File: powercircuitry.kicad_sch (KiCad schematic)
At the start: 160 parts, among them U1001 AM6231ASGGGAALW, U4001 TPS6521903RHBR, U4002 TLV62595DMQR

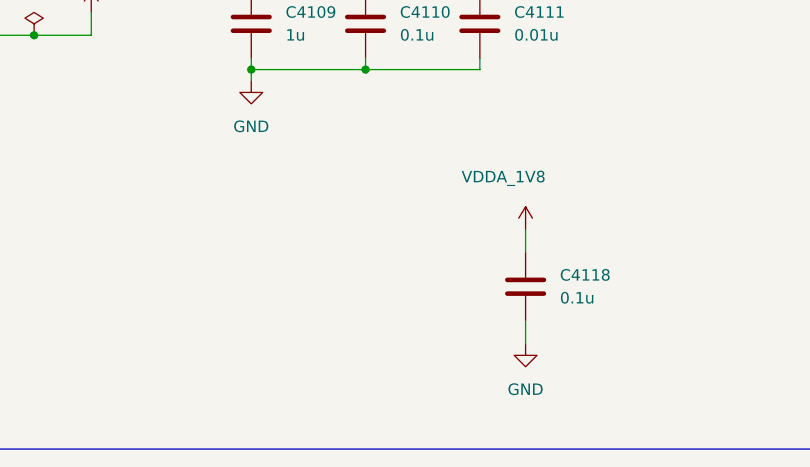
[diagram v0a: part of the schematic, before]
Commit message: More SoC decaps
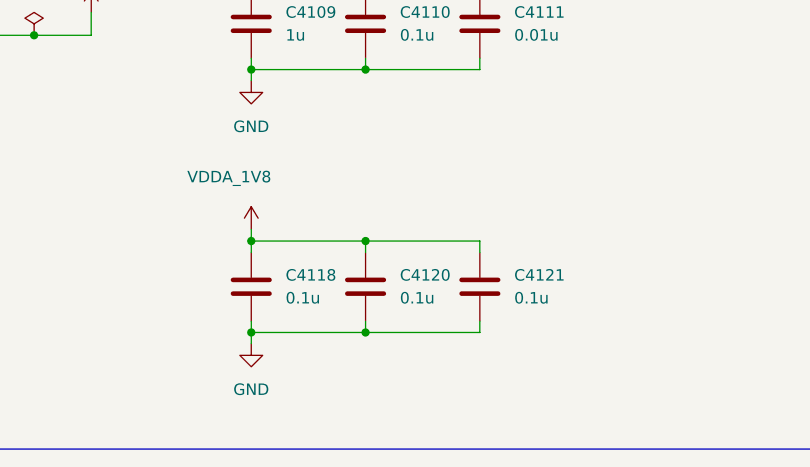
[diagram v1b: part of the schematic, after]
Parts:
- added C4120, C4121: 0.1u, Capacitor_SMD:C_0201_0603Metric, symbol Device:C
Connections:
- net GND: now also C4120.2, C4121.2
- net VDDA_1V8: now also C4120.1, C4121.1
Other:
- moved on the sheet: C4118

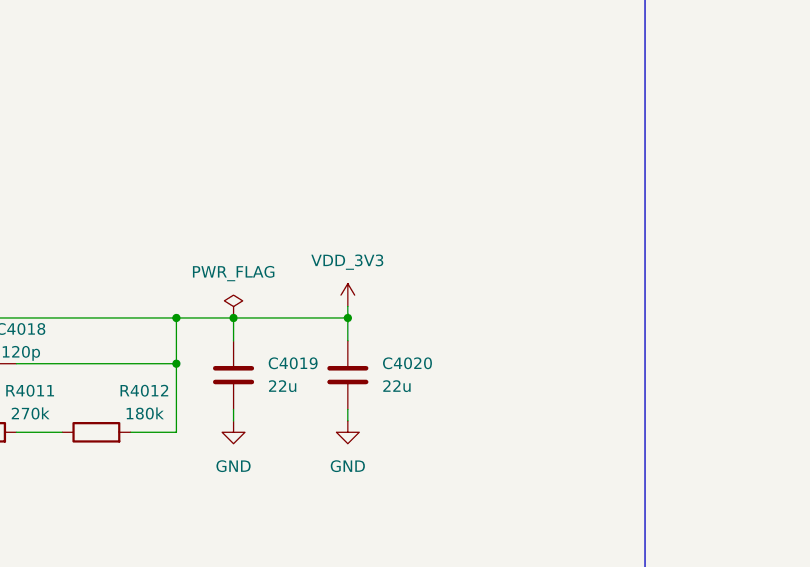
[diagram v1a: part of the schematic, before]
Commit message: Routed 5V -> 3.3V Buck converter and started PMIC routing and power planes
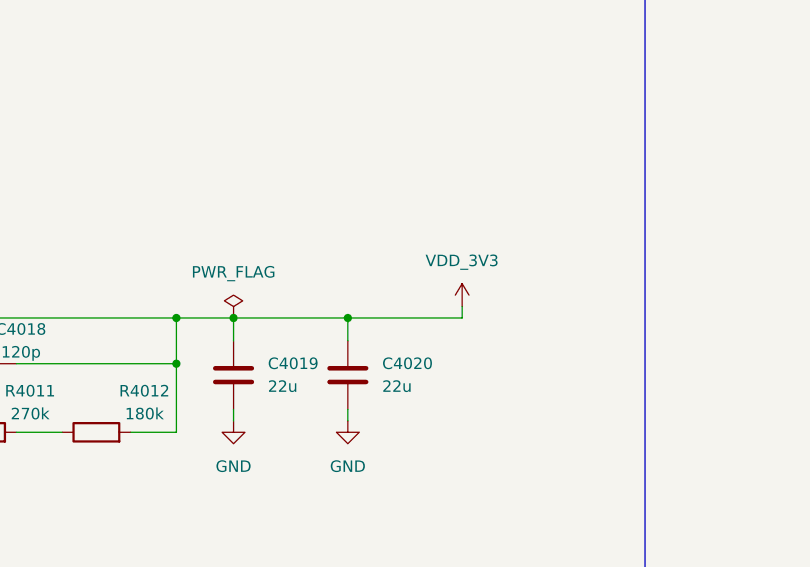
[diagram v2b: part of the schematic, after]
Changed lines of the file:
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@@
 	(wire
 		(pts
-			(xy 205.74 299.72) (xy 205.74 300.99)
+			(xy 218.44 299.72) (xy 218.44 300.99)
 		)
 		(stroke
@@
 	(wire
 		(pts
+			(xy 218.44 300.99) (xy 205.74 300.99)
+		)
+		(stroke
+			(width 0)
+			(type default)
+		)
+	)
+	(wire
+		(pts
 			(xy 538.48 431.8) (xy 538.48 434.34)
 		)
@@
 	(symbol
 		(lib_id "power:VDD")
-		(at 205.74 299.72 0)
+		(at 218.44 299.72 0)
 		(unit 1)
 		(exclude_from_sim no)
@@
 		(fields_autoplaced yes)
 		(property "Reference" "#PWR04067"
-			(at 205.74 303.53 0)
+			(at 218.44 303.53 0)
 			(effects
 				(font
@@
 		)
 		(property "Value" "VDD_3V3"
-			(at 205.74 294.64 0)
+			(at 218.44 294.64 0)
 			(effects
 				(font
@@
 		)
 		(property "Footprint" ""
-			(at 205.74 299.72 0)
+			(at 218.44 299.72 0)
 			(effects
 				(font
@@
 		)
 		(property "Datasheet" ""
-			(at 205.74 299.72 0)
+			(at 218.44 299.72 0)
 			(effects
 				(font
@@
 		)
 		(property "Description" "Power symbol creates a global label with name \"VDD\""
-			(at 205.74 299.72 0)
+			(at 218.44 299.72 0)
 			(effects
 				(font

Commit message: Routed out PMIC
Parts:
- removed C4010: 2.2u, Capacitor_SMD:C_0402_1005Metric, symbol Device:C
- removed R4001: 0R, Resistor_SMD:R_0402_1005Metric, symbol Device:R
- added C4122, C4123, C4124: 0.1u, Capacitor_SMD:C_0402_1005Metric, symbol Device:C
- C4009: value 2.2u -> 4.7u
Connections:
- net PMIC_B1_FB is gone; now on net VDD_CORE: U4001.1 (FB_B1)
- net GND: now also C4122.2, C4123.2, C4124.2
- net VSYS_5V: now also C4122.1, C4123.1, C4124.1
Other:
- moved on the sheet: C4001, C4003, C4005

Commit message: Continued PDN routing
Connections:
- net VDDA_0V85 renamed VDDR_CORE
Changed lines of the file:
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@@
 		(on_board yes)
 		(dnp no)
-		(fields_autoplaced yes)
 		(property "Reference" "#PWR04077"
 			(at 365.76 433.07 0)
@@
 			)
 		)
-		(property "Value" "VDDA_0V85"
-			(at 365.76 424.18 0)
+		(property "Value" "VDDR_CORE"
+			(at 361.442 424.18 0)
 			(effects
 				(font
 					(size 1.27 1.27)
 				)
+				(justify left)
 			)
 		)
@@
 		(on_board yes)
 		(dnp no)
-		(fields_autoplaced yes)
 		(property "Reference" "#PWR04020"
 			(at 414.02 182.88 0)
@@
 			)
 		)
-		(property "Value" "VDDA_0V85"
-			(at 414.02 173.99 0)
+		(property "Value" "VDDR_CORE"
+			(at 409.194 174.244 0)
 			(effects
 				(font
 					(size 1.27 1.27)
 				)
+				(justify left)
 			)
 		)
@@
 			)
 		)
-		(property "Value" "VDDA_0V85"
+		(property "Value" "VDDR_CORE"
 			(at 234.188 191.516 0)
 			(effects

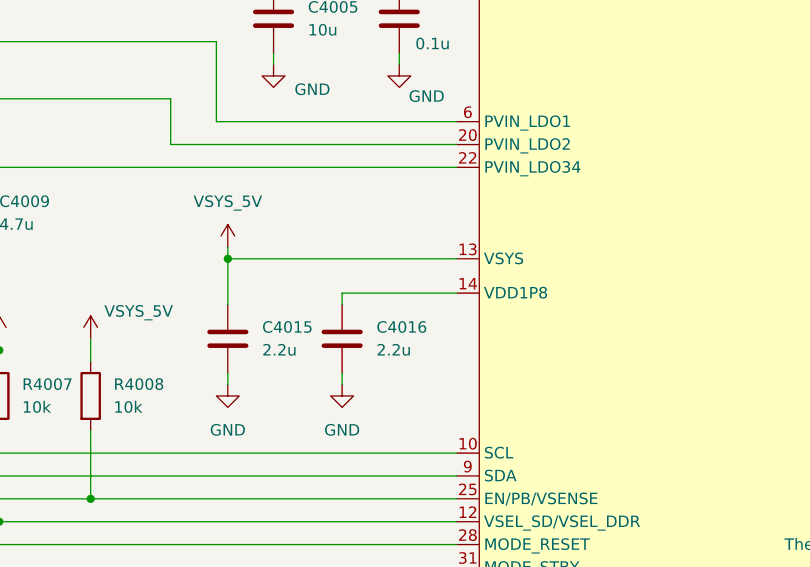
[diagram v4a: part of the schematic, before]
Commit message: Improved clock layout and clock PDN
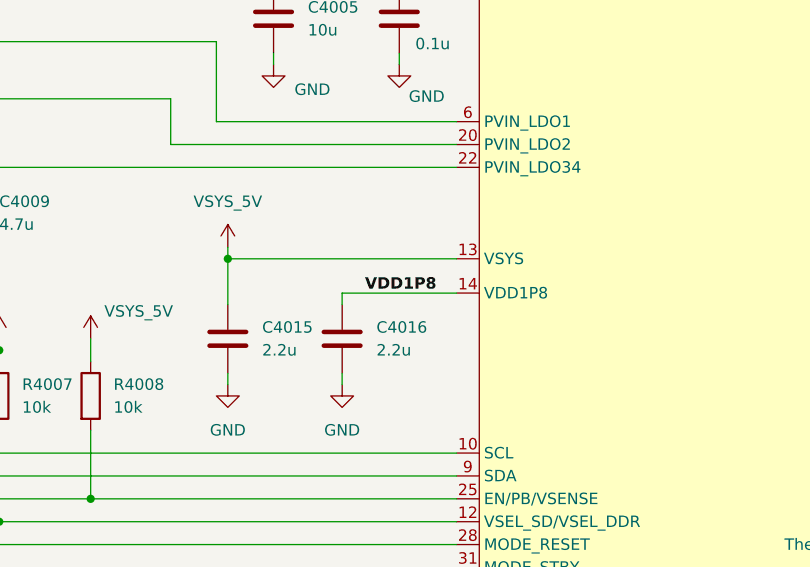
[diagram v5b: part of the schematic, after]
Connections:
- net VDD1P8: now reaches C4016.1, U4001.14 (VDD1P8)
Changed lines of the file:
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@@
+		)
+	)
+	(label "VDD1P8"
+		(at 154.94 214.63 0)
+		(effects
+			(font
+				(size 1.27 1.27)
+				(thickness 0.254)
+				(bold yes)
+			)
+			(justify left bottom)
 		)
 	)

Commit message: Added new radio schematic
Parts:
- renumbered C4001 to C3001, C4122 to C3002, C4002 to C3003, C4003 to C3004, C4123 to C3005, C4004 to C3006, C4005 to C3007, C4124 to C3008, C4006 to C3009, C4007 to C3010, C4008 to C3011, C4009 to C3012, C4011 to C3013, C4012 to C3014, C4013 to C3015, C4014 to C3016, C4015 to C3017, C4016 to C3018, C4017 to C3019, C4018 to C3020, C4019 to C3021, C4020 to C3022, C4021 to C3023, C4022 to C3024, C4023 to C3025, C4024 to C3026, C4025 to C3027, C4026 to C3028, C4027 to C3029, C4028 to C3030, C4029 to C3031, C4030 to C3032, C4031 to C3033, C4032 to C3034, C4033 to C3035, C4034 to C3036, C4035 to C3037, C4036 to C3038, C4037 to C3039, C4038 to C3040, C4039 to C3041, C4040 to C3042, C4041 to C3043, C4042 to C3044, C4043 to C3045, C4044 to C3046, C4045 to C3047, C4046 to C3048, C4047 to C3049, C4048 to C3050, C4049 to C3051, C4050 to C3052, C4051 to C3053, C4052 to C3054, C4053 to C3055, C4054 to C3056, C4055 to C3057, C4056 to C3058, C4057 to C3059, C4058 to C3060, C4059 to C3061, C4060 to C3062, C4061 to C3063, C4062 to C3064, C4063 to C3065, C4064 to C3066, C4065 to C3067, C4066 to C3068, C4067 to C3069, C4068 to C3070, C4069 to C3071, C4070 to C3072, C4071 to C3073, C4072 to C3074, C4073 to C3075, C4074 to C3076, C4075 to C3077, C4076 to C3078, C4077 to C3079, C4078 to C3080, C4079 to C3081, C4080 to C3082, C4081 to C3083, C4082 to C3084, C4083 to C3085, C4084 to C3086, C4085 to C3087, C4086 to C3088, C4087 to C3089, C4088 to C3090, C4089 to C3091, C4090 to C3092, C4091 to C3093, C4092 to C3094, C4093 to C3095, C4094 to C3096, C4095 to C3097, C4096 to C3098, C4097 to C3099, C4098 to C3100, C4099 to C3101, C4100 to C3102, C4101 to C3103, C4102 to C3104, C4103 to C3105, C4104 to C3106, C4105 to C3107, C4106 to C3108, C4107 to C3109, C4108 to C3110, C4109 to C3111, C4110 to C3112, C4111 to C3113, C4112 to C3114, C4113 to C3115, C4114 to C3116, C4115 to C3117, C4116 to C3118, C4117 to C3119, C4118 to C3120, C4120 to C3121, C4121 to C3122, C4119 to C3123, FB4001 to FB3001, FB4002 to FB3002, FB4003 to FB3003, FB4004 to FB3004, FB4005 to FB3005, FB4006 to FB3006, FB4007 to FB3007, FB4008 to FB3008, FB4009 to FB3009, FB4010 to FB3010, FB4011 to FB3011, L4001 to L3001, L4002 to L3002, L4003 to L3003, L4004 to L3004, R4002 to R3001, R4003 to R3002, R4004 to R3003, R4005 to R3004, R4006 to R3005, R4007 to R3006, R4008 to R3007, R4014 to R3008, R4015 to R3009, R4009 to R3010, R4010 to R3011, R4011 to R3012, R4012 to R3013, R4013 to R3014, TP4002 to TP3001, TP4003 to TP3002, TP4004 to TP3003, TP4005 to TP3004, TP4006 to TP3005, TP4007 to TP3006, TP4008 to TP3007, TP4001 to TP3008, U1001 to U1002, U4001 to U3001, U4002 to U3002

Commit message: Routed all power rails to AM6231 SoC
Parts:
- C3108, C3111: footprint Capacitor_SMD:C_0201_0603Metric -> Capacitor_SMD:C_0402_1005Metric
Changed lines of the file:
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@@
 			)
 		)
-		(property "Footprint" "Capacitor_SMD:C_0201_0603Metric"
+		(property "Footprint" "Capacitor_SMD:C_0402_1005Metric"
 			(at 510.2352 586.74 0)
 			(effects
@@
 			)
 		)
-		(property "Footprint" "Capacitor_SMD:C_0201_0603Metric"
+		(property "Footprint" "Capacitor_SMD:C_0402_1005Metric"
 			(at 414.9852 586.74 0)
 			(effects

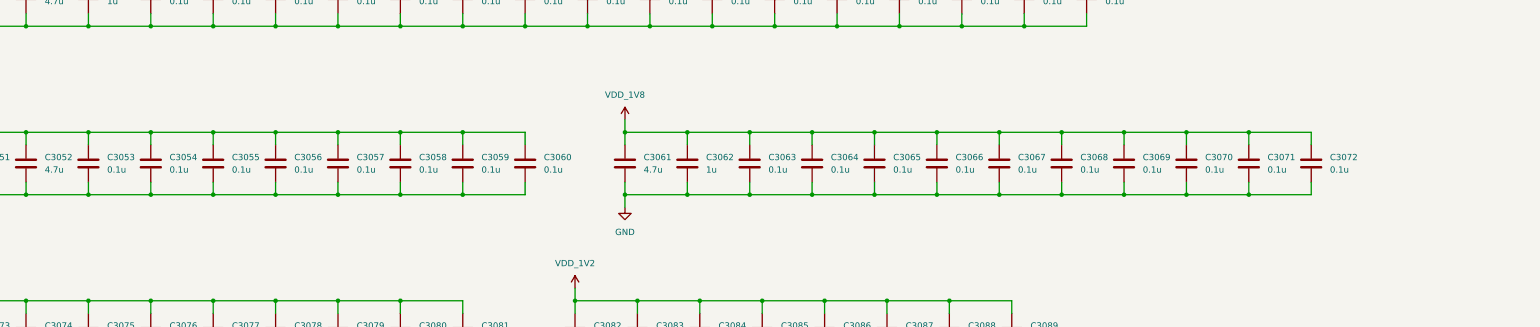
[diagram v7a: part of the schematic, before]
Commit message: Placed bulk decaps for VDDR_CORE and VDD_CORE
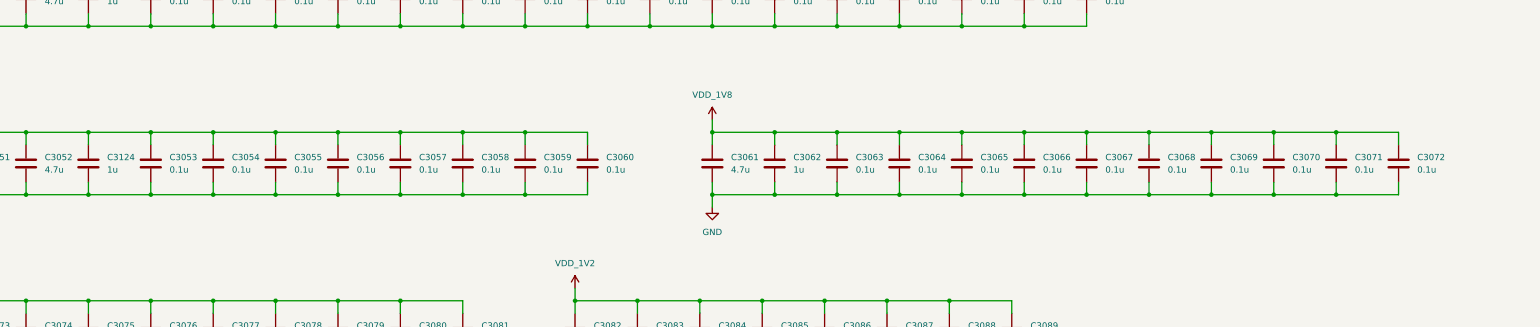
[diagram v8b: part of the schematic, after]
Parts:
- added C3124: 1u, SoftServicesFootprintLibrary:0201_Cap_Leonhart, symbol Device:C
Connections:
- net GND: now also C3124.2
- net VDDR_CORE: now also C3124.1
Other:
- moved on the sheet: C3053, C3054, C3055, C3056, C3057, C3058, C3059, C3060, C3061, C3062, C3063, C3064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
